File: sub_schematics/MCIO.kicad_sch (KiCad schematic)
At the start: 1 part

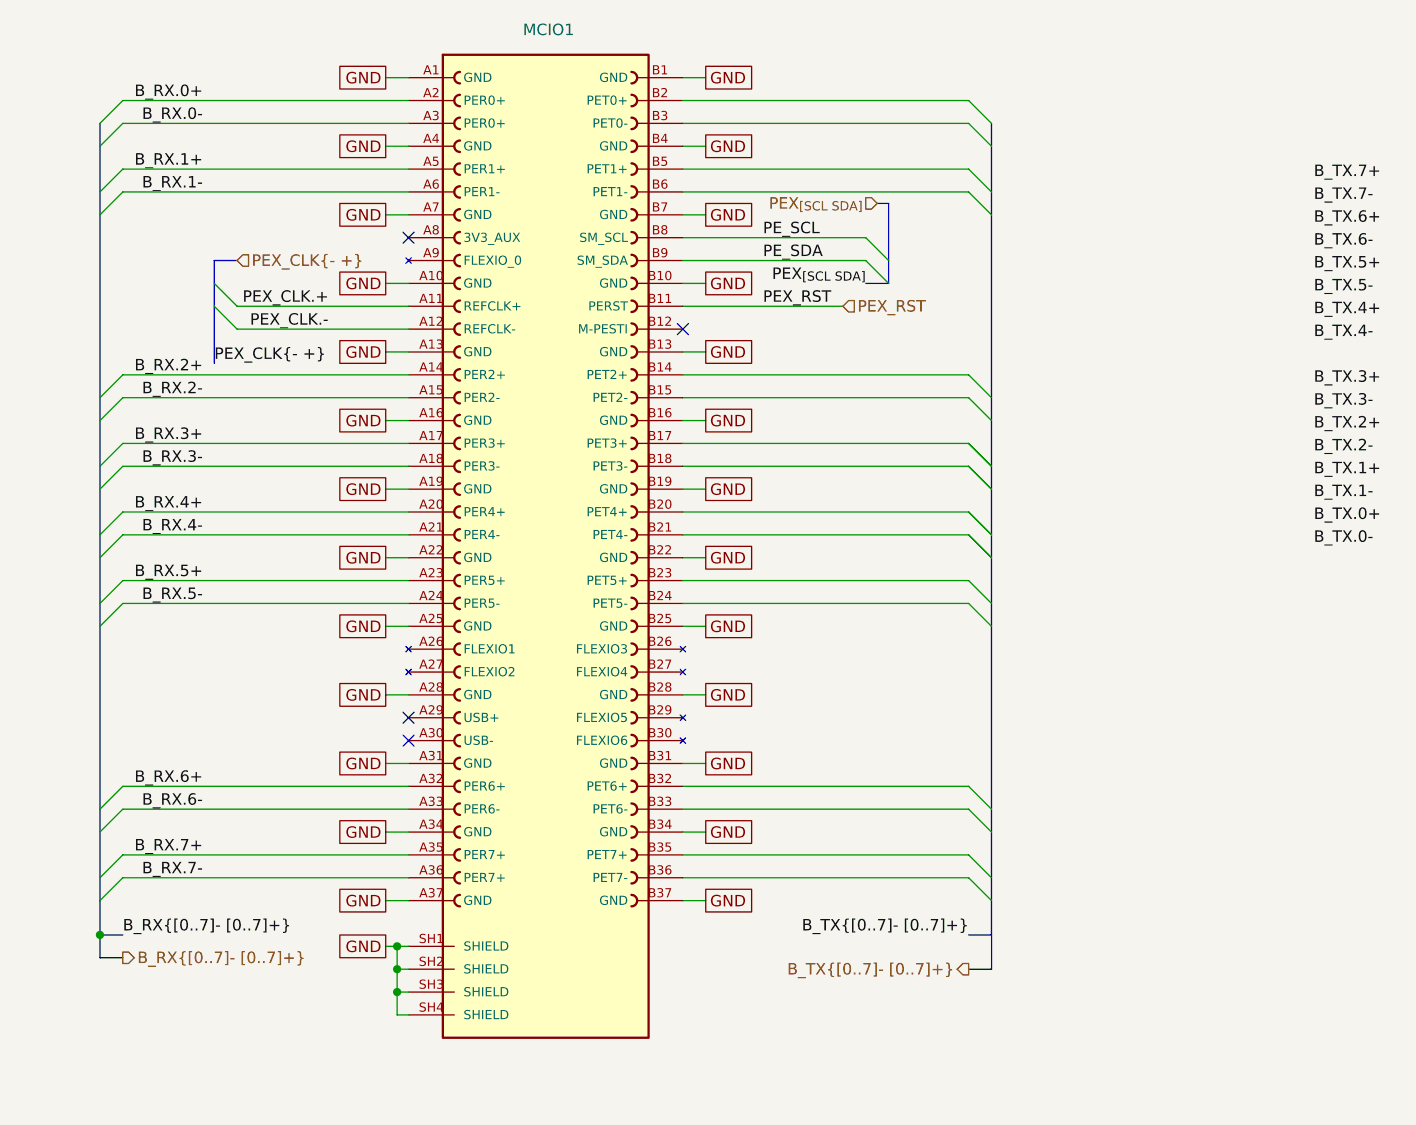
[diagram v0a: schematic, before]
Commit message: Schematics revamped
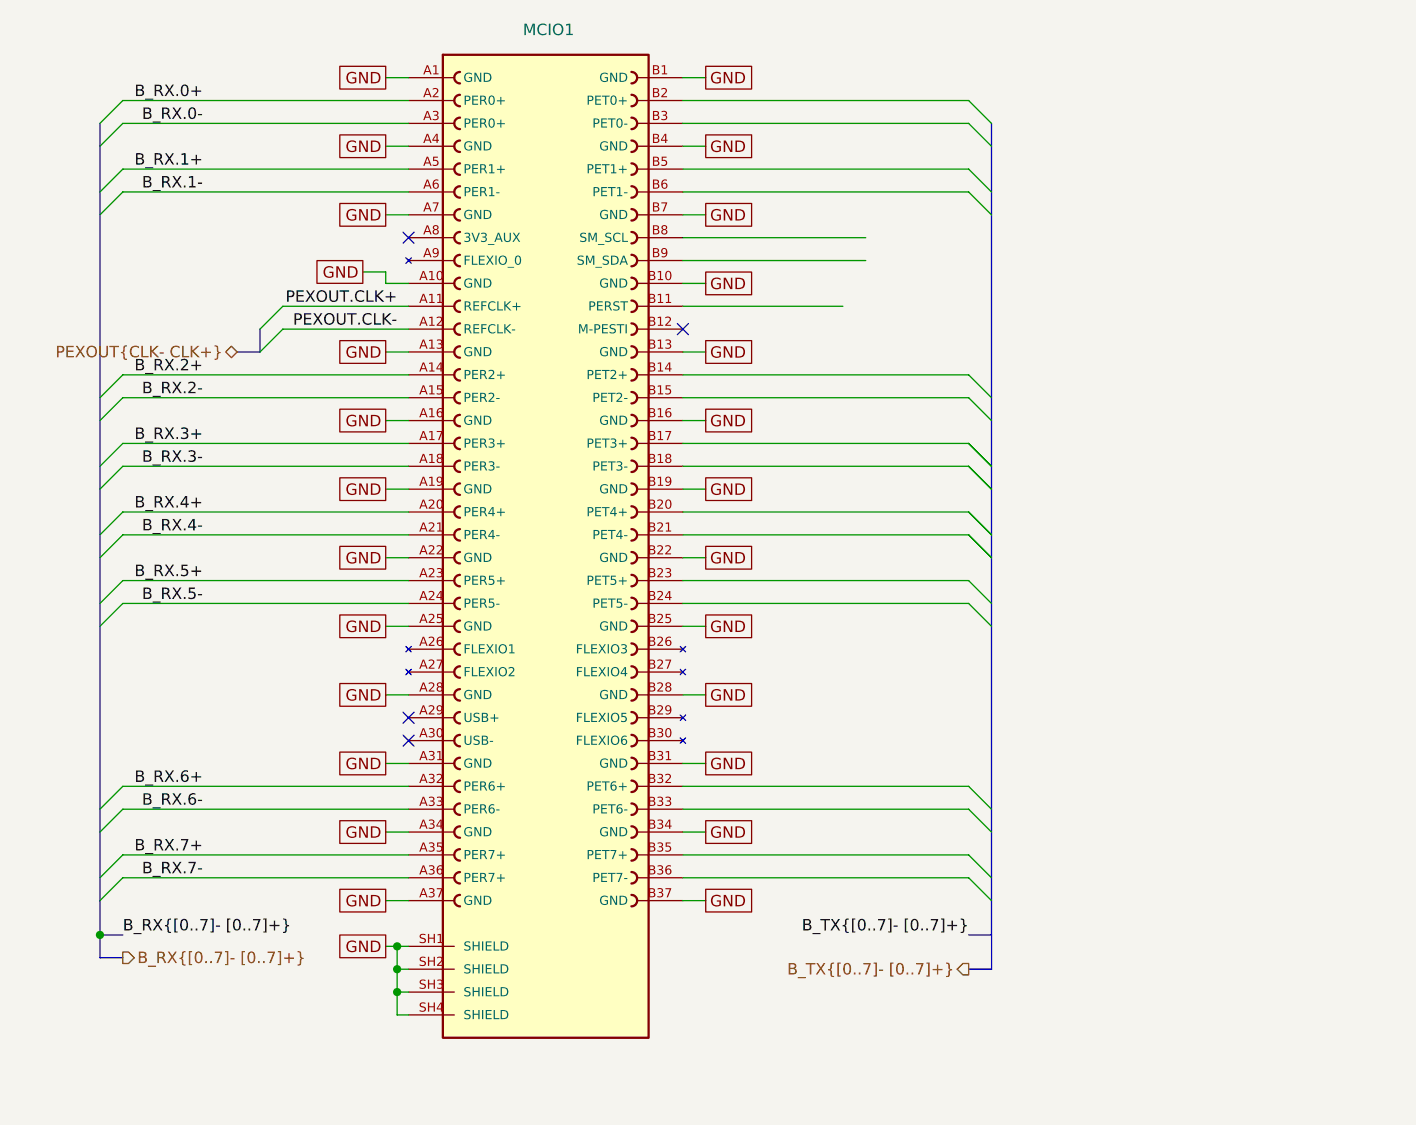
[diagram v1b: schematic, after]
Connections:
- net PEX_CLK.+ renamed PEXOUT.CLK+
- net PEX_CLK.- renamed PEXOUT.CLK-
- net PEX_RST: no longer names the net of MCIO1.B11 (PERST)
- net PE_SCL: no longer names the net of MCIO1.B8 (SM_SCL)
- net PE_SDA: no longer names the net of MCIO1.B9 (SM_SDA)

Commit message: PCIe shematic fix
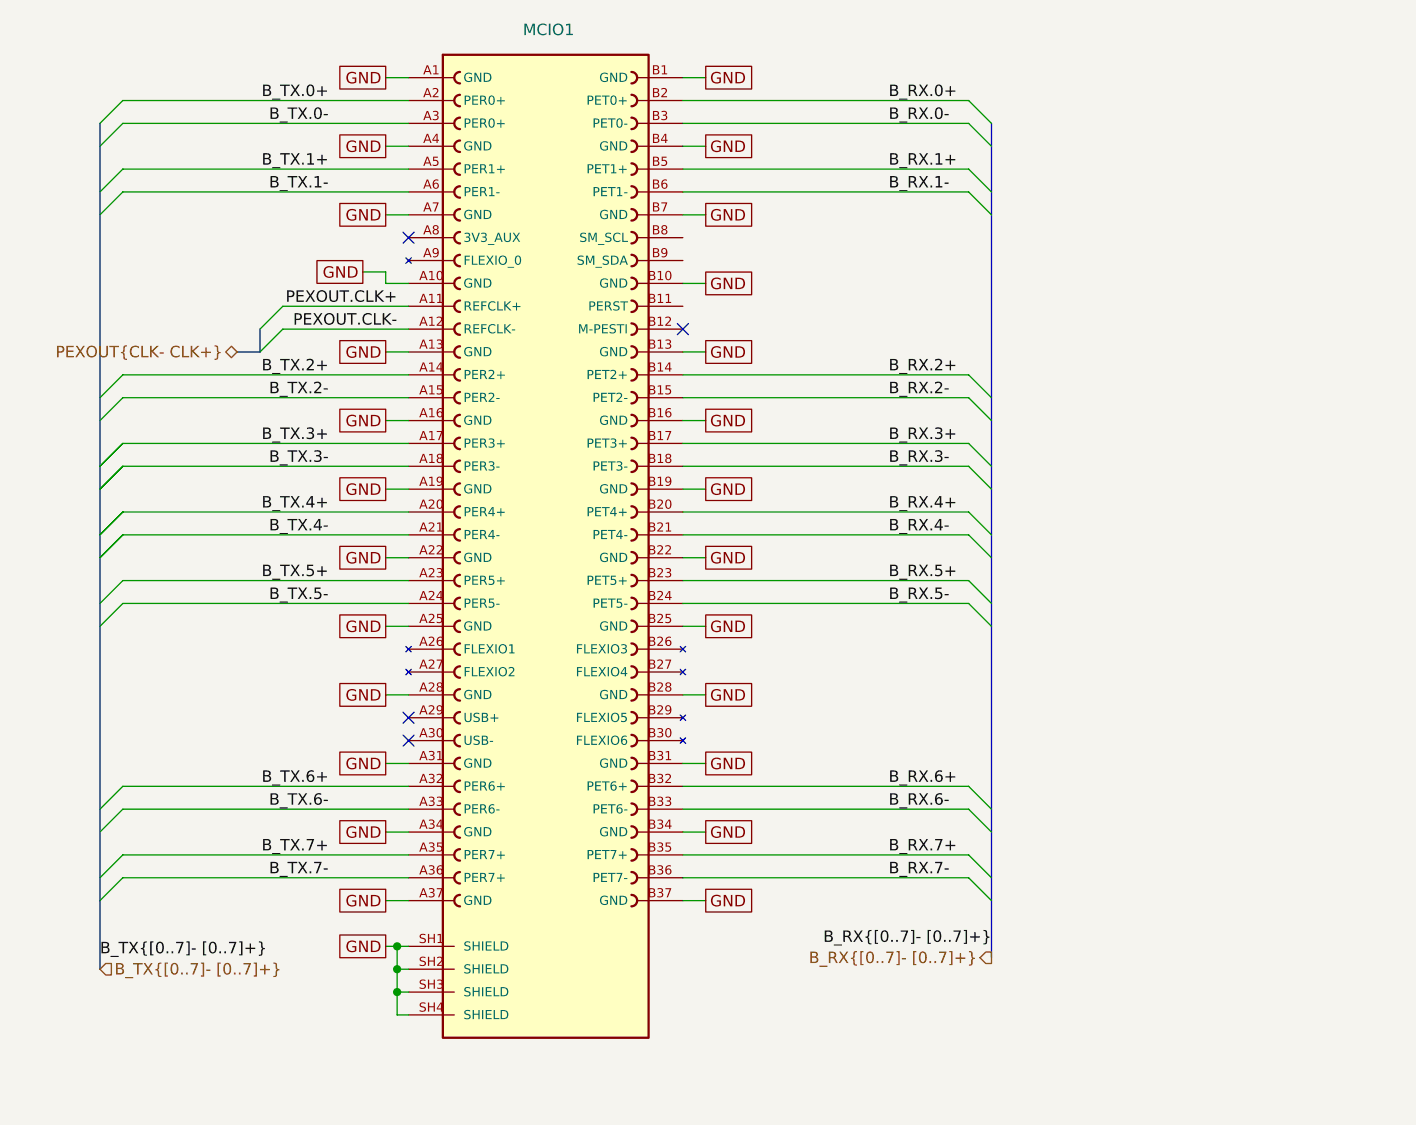
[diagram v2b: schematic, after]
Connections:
- net B_RX.0+: now also MCIO1.B2 (PET0+); no longer MCIO1.A2 (PER0+)
- net B_RX.0-: now also MCIO1.B3 (PET0-); no longer MCIO1.A3 (PER0+)
- net B_RX.1+: now also MCIO1.B5 (PET1+); no longer MCIO1.A5 (PER1+)
- net B_RX.1-: now also MCIO1.B6 (PET1-); no longer MCIO1.A6 (PER1-)
- net B_RX.2+: now also MCIO1.B14 (PET2+); no longer MCIO1.A14 (PER2+)
- net B_RX.2-: now also MCIO1.B15 (PET2-); no longer MCIO1.A15 (PER2-)
- net B_RX.3+: now also MCIO1.B17 (PET3+); no longer MCIO1.A17 (PER3+)
- net B_RX.3-: now also MCIO1.B18 (PET3-); no longer MCIO1.A18 (PER3-)
- net B_RX.4+: now also MCIO1.B20 (PET4+); no longer MCIO1.A20 (PER4+)
- net B_RX.4-: now also MCIO1.B21 (PET4-); no longer MCIO1.A21 (PER4-)
- net B_RX.5+: now also MCIO1.B23 (PET5+); no longer MCIO1.A23 (PER5+)
- net B_RX.5-: now also MCIO1.B24 (PET5-); no longer MCIO1.A24 (PER5-)
- net B_RX.6+: now also MCIO1.B32 (PET6+); no longer MCIO1.A32 (PER6+)
- net B_RX.6-: now also MCIO1.B33 (PET6-); no longer MCIO1.A33 (PER6-)
- net B_RX.7+: now also MCIO1.B35 (PET7+); no longer MCIO1.A35 (PER7+)
- net B_RX.7-: now also MCIO1.B36 (PET7-); no longer MCIO1.A36 (PER7+)
- new net B_TX.0+: MCIO1.A2 (PER0+)
- new net B_TX.0-: MCIO1.A3 (PER0+)
- new net B_TX.1+: MCIO1.A5 (PER1+)
- new net B_TX.1-: MCIO1.A6 (PER1-)
- new net B_TX.2+: MCIO1.A14 (PER2+)
- new net B_TX.2-: MCIO1.A15 (PER2-)
- new net B_TX.3+: MCIO1.A17 (PER3+)
- new net B_TX.3-: MCIO1.A18 (PER3-)
- new net B_TX.4+: MCIO1.A20 (PER4+)
- new net B_TX.4-: MCIO1.A21 (PER4-)
- new net B_TX.5+: MCIO1.A23 (PER5+)
- new net B_TX.5-: MCIO1.A24 (PER5-)
- new net B_TX.6+: MCIO1.A32 (PER6+)
- new net B_TX.6-: MCIO1.A33 (PER6-)
- new net B_TX.7+: MCIO1.A35 (PER7+)
- new net B_TX.7-: MCIO1.A36 (PER7+)

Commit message: Switch to retimer for only clock
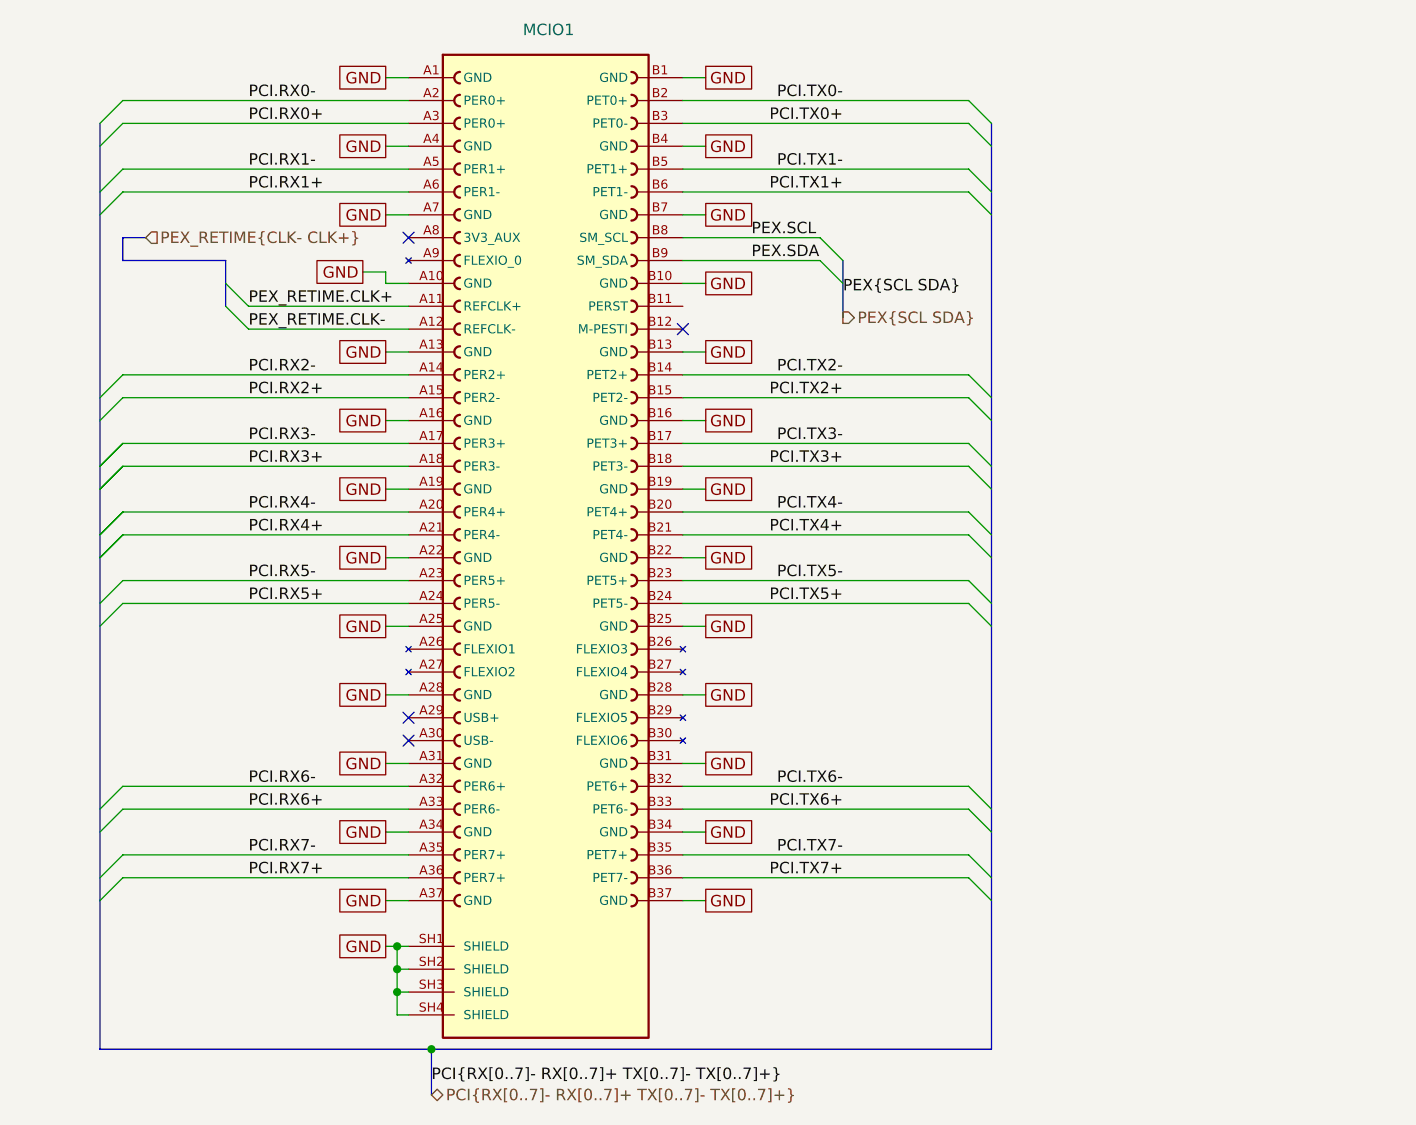
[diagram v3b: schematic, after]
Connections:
- net PEX.SCL: now reaches MCIO1.B8 (SM_SCL)
- net PEX.SDA: now reaches MCIO1.B9 (SM_SDA)
- net B_RX.0+ renamed PCI.TX0-
- net B_RX.0- renamed PCI.TX0+
- net B_RX.1+ renamed PCI.TX1-
- net B_RX.1- renamed PCI.TX1+
- net B_RX.2+ renamed PCI.TX2-
- net B_RX.2- renamed PCI.TX2+
- net B_RX.3+ renamed PCI.TX3-
- net B_RX.3- renamed PCI.TX3+
- net B_RX.4+ renamed PCI.TX4-
- net B_RX.4- renamed PCI.TX4+
- net B_RX.5+ renamed PCI.TX5-
- net B_RX.5- renamed PCI.TX5+
- net B_RX.6+ renamed PCI.TX6-
- net B_RX.6- renamed PCI.TX6+
- net B_RX.7+ renamed PCI.TX7-
- net B_RX.7- renamed PCI.TX7+
- net B_TX.0+ renamed PCI.RX0-
- net B_TX.0- renamed PCI.RX0+
- net B_TX.1+ renamed PCI.RX1-
- net B_TX.1- renamed PCI.RX1+
- net B_TX.2+ renamed PCI.RX2-
- net B_TX.2- renamed PCI.RX2+
- net B_TX.3+ renamed PCI.RX3-
- net B_TX.3- renamed PCI.RX3+
- net B_TX.4+ renamed PCI.RX4-
- net B_TX.4- renamed PCI.RX4+
- net B_TX.5+ renamed PCI.RX5-
- net B_TX.5- renamed PCI.RX5+
- net B_TX.6+ renamed PCI.RX6-
- net B_TX.6- renamed PCI.RX6+
- net B_TX.7+ renamed PCI.RX7-
- net B_TX.7- renamed PCI.RX7+
- net PEXOUT.CLK+ renamed PEX_RETIME.CLK+
- net PEXOUT.CLK- renamed PEX_RETIME.CLK-

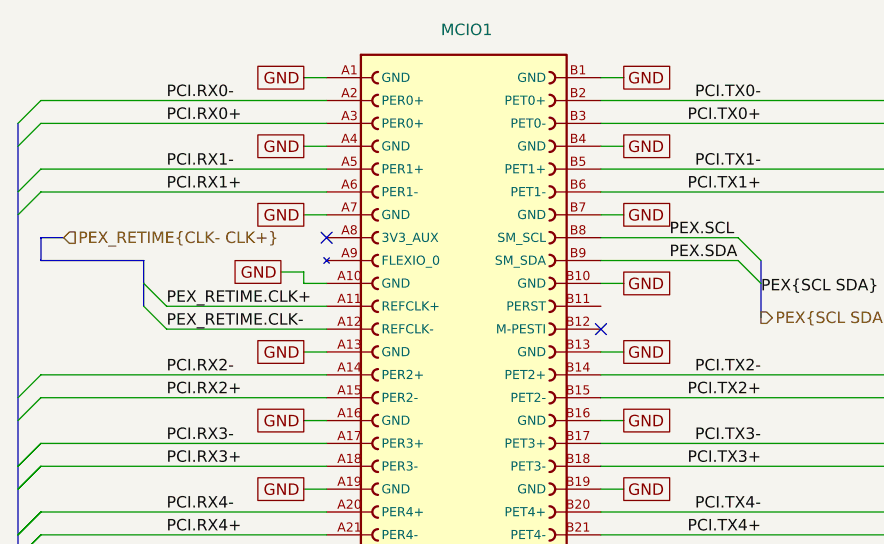
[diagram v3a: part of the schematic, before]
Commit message: Fixed board dimensions
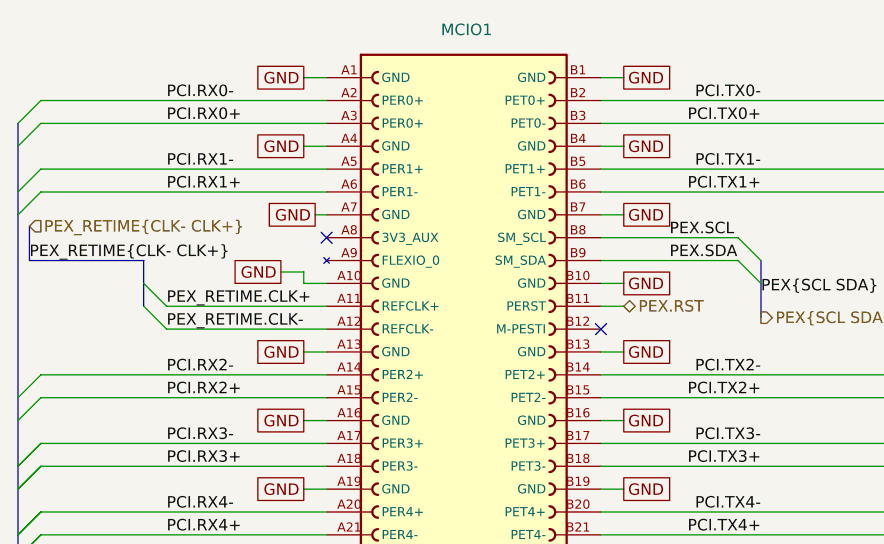
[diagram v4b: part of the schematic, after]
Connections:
- net PEX.RST: now reaches MCIO1.B11 (PERST)
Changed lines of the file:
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@@
 	(bus
 		(pts
-			(xy 44.45 55.88) (xy 33.02 55.88)
+			(xy 44.45 55.88) (xy 31.75 55.88)
 		)
 		(stroke
@@
 	(wire
 		(pts
+			(xy 95.25 60.96) (xy 97.79 60.96)
+		)
+		(stroke
+			(width 0)
+			(type default)
+		)
+	)
+	(wire
+		(pts
 			(xy 127 45.72) (xy 95.25 45.72)
 		)
@@
 		)
 	)
+	(wire
+		(pts
+			(xy 127 48.26) (xy 95.25 48.26)
+		)
+		(stroke
+			(width 0)
+			(type default)
+		)
+	)
+	(wire
+		(pts
+			(xy 63.5 134.62) (xy 63.5 132.08)
+		)
+		(stroke
+			(width 0)
+			(type default)
+		)
+	)
+	(wire
+		(pts
+			(xy 97.79 104.14) (xy 95.25 104.14)
+		)
+		(stroke
+			(width 0)
+			(type default)
+		)
+	)
 	(bus
 		(pts
-			(xy 35.56 53.34) (xy 33.02 53.34)
-		)
-		(stroke
-			(width 0)
-			(type default)
-		)
-	)
-	(wire
-		(pts
-			(xy 127 48.26) (xy 95.25 48.26)
-		)
-		(stroke
-			(width 0)
-			(type default)
-		)
-	)
-	(wire
-		(pts
-			(xy 63.5 134.62) (xy 63.5 132.08)
-		)
-		(stroke
-			(width 0)
-			(type default)
-		)
-	)
-	(wire
-		(pts
-			(xy 97.79 104.14) (xy 95.25 104.14)
+			(xy 30.48 127) (xy 30.48 143.51)
+		)
+		(stroke
+			(width 0)
+			(type default)
+		)
+	)
+	(wire
+		(pts
+			(xy 63.5 50.8) (xy 64.77 50.8)
+		)
+		(stroke
+			(width 0)
+			(type default)
+		)
+	)
+	(wire
+		(pts
+			(xy 95.25 124.46) (xy 127 124.46)
+		)
+		(stroke
+			(width 0)
+			(type default)
+		)
+	)
+	(wire
+		(pts
+			(xy 64.77 38.1) (xy 33.02 38.1)
+		)
+		(stroke
+			(width 0)
+			(type default)
+		)
+	)
+	(wire
+		(pts
+			(xy 62.23 88.9) (xy 64.77 88.9)
 		)
 		(stroke
@@
 	(bus
 		(pts
-			(xy 30.48 127) (xy 30.48 143.51)
-		)
-		(stroke
-			(width 0)
-			(type default)
-		)
-	)
-	(wire
-		(pts
-			(xy 62.23 50.8) (xy 64.77 50.8)
-		)
-		(stroke
-			(width 0)
-			(type default)
-		)
-	)
-	(wire
-		(pts
-			(xy 95.25 124.46) (xy 127 124.46)
-		)
-		(stroke
-			(width 0)
-			(type default)
-		)
-	)
-	(wire
-		(pts
-			(xy 64.77 38.1) (xy 33.02 38.1)
-		)
-		(stroke
-			(width 0)
-			(type default)
-		)
-	)
-	(wire
-		(pts
-			(xy 62.23 88.9) (xy 64.77 88.9)
+			(xy 129.54 40.64) (xy 129.54 127)
 		)
 		(stroke
@@
 	(bus
 		(pts
-			(xy 129.54 40.64) (xy 129.54 127)
+			(xy 31.75 52.07) (xy 31.75 55.88)
 		)
 		(stroke
@@
 		(pts
 			(xy 113.03 55.88) (xy 113.03 62.23)
-		)
-		(stroke
-			(width 0)
-			(type default)
-		)
-	)
-	(bus
-		(pts
-			(xy 33.02 55.88) (xy 33.02 53.34)
 		)
 		(stroke
@@
 		)
 	)
+	(label "PEX_RETIME{CLK- CLK+}"
+		(at 31.75 55.88 0)
+		(effects
+			(font
+				(size 1.27 1.27)
+			)
+			(justify left bottom)
+		)
+	)
 	(label "PCI.TX6-"
 		(at 113.03 114.3 180)
@@
 	(global_label "GND"
 		(shape passive)
-		(at 62.23 50.8 180)
+		(at 63.5 50.8 180)
 		(fields_autoplaced yes)
 		(effects
@@
 		)
 		(property "Intersheetrefs" "${INTERSHEET_REFS}"
-			(at 56.4856 50.8 0)
+			(at 57.7556 50.8 0)
 			(hide yes)
 			(show_name no)
@@
 				(justify left)
 			)
+		)
+	)
+	(hierarchical_label "PEX_RETIME{CLK- CLK+}"
+		(shape input)
+		(at 31.75 52.07 0)
+		(effects
+			(font
+				(size 1.27 1.27)
+			)
+			(justify left)
 		)
 	)
@@
 		)
 	)
-	(hierarchical_label "PEX_RETIME{CLK- CLK+}"
-		(shape input)
-		(at 35.56 53.34 0)
-		(effects
-			(font
+	(hierarchical_label "PEX.RST"
+		(shape bidirectional)
+		(at 97.79 60.96 0)
+		(effects
+			(font

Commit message: Order prepare
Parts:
- MCIO1: JLCPCB Part # (none) -> C4499806; LCSC Part # C4499806 -> (none)
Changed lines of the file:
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@@
 			)
 		)
-		(property "LCSC Part #" "C4499806"
+		(property "JLCPCB Part #" "C4499806"
 			(at 80.01 87.63 0)
 			(hide yes)
